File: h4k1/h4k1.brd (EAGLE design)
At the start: 250 x 80 mm, 202 parts, among them IC1 STM32F10XCXT6, J2 PJ-313D-AUDIO-JACK, J3 USB-AF10, K1 CHERRY-MX-LED, K10 CHERRY-MX, K11 CHERRY-MX, K12 CHERRY-MX, K13 CHERRY-MX, K14 CHERRY-MX, K15 CHERRY-MX, K16 CHERRY-MX, K17 CHERRY-MX-LED, K18 CHERRY-MX, K19 CHERRY-MX, K2 CHERRY-MX-LED, K20 CHERRY-MX, K21 CHERRY-MX, K22 CHERRY-MX, K23 CHERRY-MX, K24 CHERRY-MX, K25 CHERRY-MX-LED, K26 CHERRY-MX, K27 CHERRY-MX, K28 CHERRY-MX, K29 CHERRY-MX, K3 CHERRY-MX-LED, K30 CHERRY-MX, K31 CHERRY-MX, K32 CHERRY-MX, K33 CHERRY-MX-LED, K34 CHERRY-MX, K35 CHERRY-MX, K36 CHERRY-MX-LED, K37 CHERRY-MX-LED, K38 CHERRY-MX, K39 CHERRY-MX, K4 CHERRY-MX-LED, K40 CHERRY-MX-LED, K41 CHERRY-MX, K42 CHERRY-MX, K43 CHERRY-MX, K44 CHERRY-MX, K45 CHERRY-MX, K46 CHERRY-MX-LED, K5 CHERRY-MX-LED, K6 CHERRY-MX-LED, K65 EVQPUL02K, K66 EVQPUL02K, K67 K3-1280S-F2, K7 CHERRY-MX-LED, K8 CHERRY-MX-LED, K9 CHERRY-MX-LED, T1 DBG, U1 GL850G, U3 PCM2704CDB, U4 74HC138, X3 12MHz, X4 12MHz

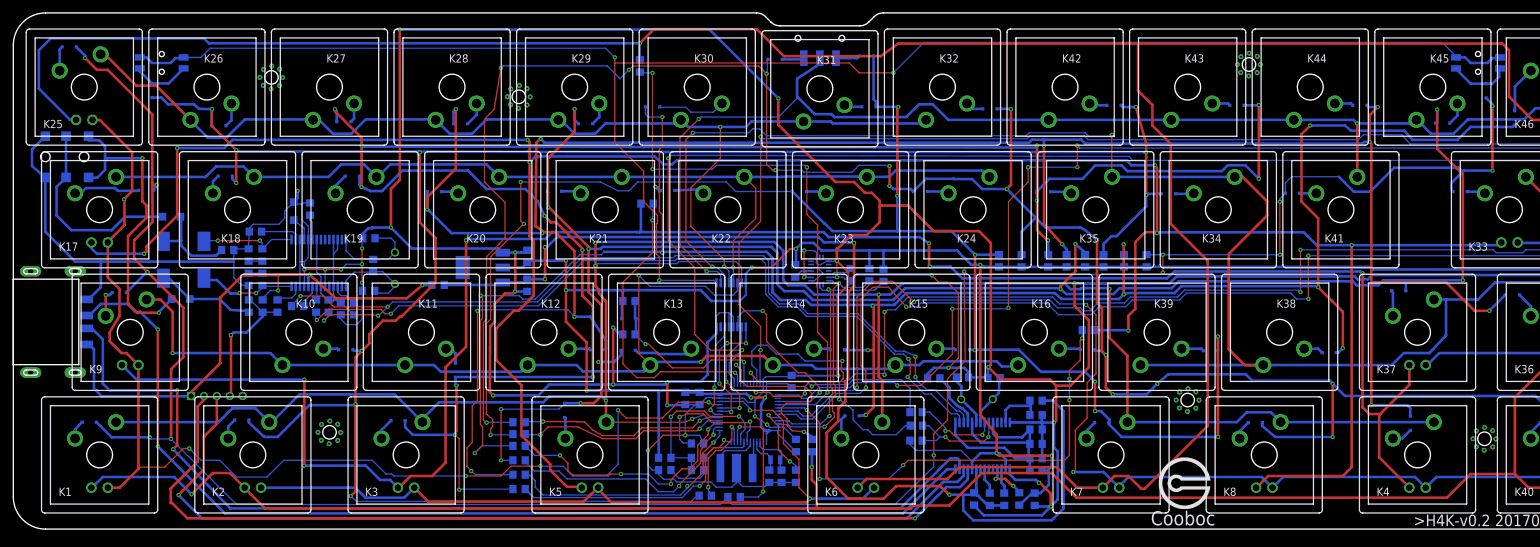
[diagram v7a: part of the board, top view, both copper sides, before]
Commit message: add usb disconnect pin
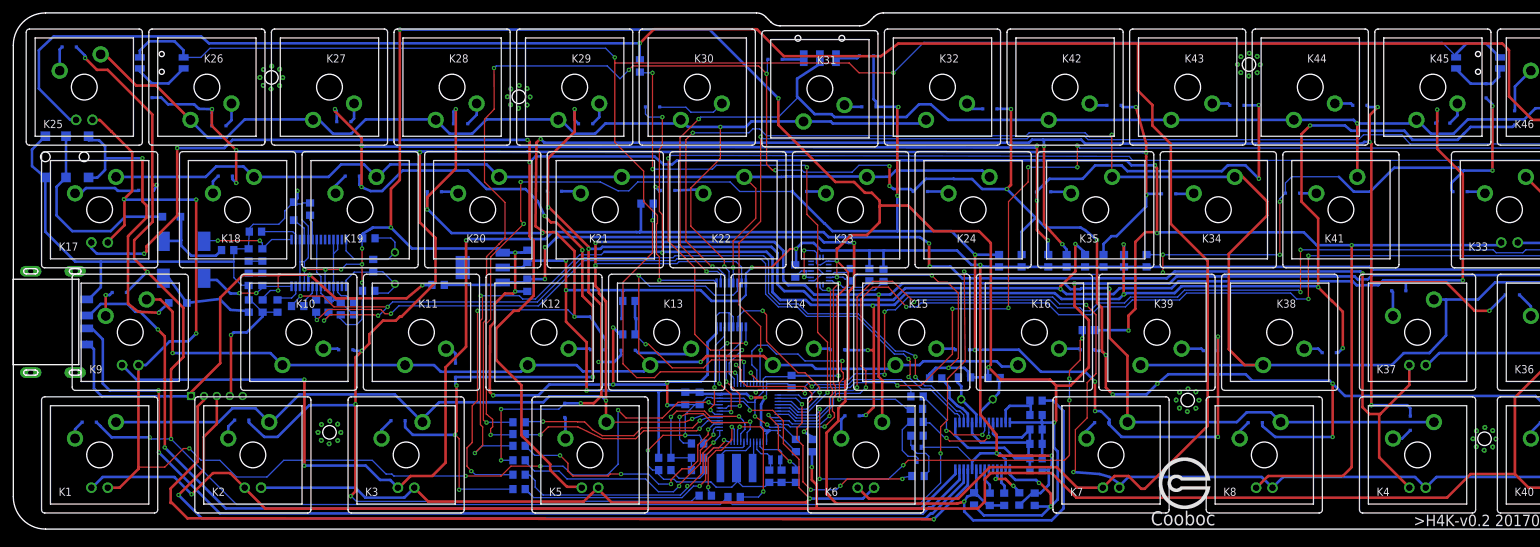
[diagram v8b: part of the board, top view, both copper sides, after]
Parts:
- added R44: 10k, hqc:0805
- added R45: 2.2k, hqc:0805
- added U5: SS8550-SOT-323, hqc:SOT-323
- moved R24 2.90 mm to (140.1, 16.6)
- moved R38 2.59 mm to (140.0, 18.6)
- moved R37 2.44 mm to (140.1, 20.6)
- moved C32 0.76 mm to (25.5, 35.1)
- moved C10 0.30 mm to (147.4, 23.5)
- moved R20 0.30 mm to (143.0, 23.4)
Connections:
- new net N$87: R44.P$2, R45.P$2, U5.P$1
- new net N$91: R24.P$1, U5.P$3
- new net USB_DISC: IC1.38, R45.P$1
- net VDD: now also R44.P$1, U5.P$2; no longer R24.P$1
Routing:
- net USB_DISC: track 0.00 -> 35.2 mm, vias 0 -> 4
- net LED_C1: track 175.9 -> 196.4 mm, vias 6 -> 8
- net N$91: track 0.00 -> 8.54 mm
- net N$87: track 0.00 -> 8.50 mm
- net N$81: track 31.9 -> 26.1 mm
- net KB_R7: track 263.7 -> 268.0 mm
- net N$74: track 41.8 -> 38.7 mm
- net N$72: track 32.9 -> 29.8 mm
- net N$80: track 76.5 -> 78.7 mm
- net N$2: track 366.7 -> 368.8 mm
- net LED_R4: track 265.5 -> 267.6 mm
- net USB3-: track 13.1 -> 14.7 mm
- net LED_R1: track 389.9 -> 391.4 mm
- net RS_A2: track 29.9 -> 31.2 mm
- net USB1-: track 161.9 -> 160.6 mm
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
